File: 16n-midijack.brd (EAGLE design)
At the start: 248.9 x 120.7 mm, 108 parts, among them J1 PJ302M, J10 PJ302M, J11 PJ302M, J12 PJ302M, J13 PJ302M, J14 PJ302M, J15 PJ302M, J16 PJ302M, J2 PJ302M, J3 PJ302M, J4 PJ302M, J5 PJ302M, J6 PJ302M, J7 PJ302M, J8 PJ302M, J9 PJ302M, U1 MCP6004_SMD, U2 MCP6004_SMD, U3 MCP6004_SMD, U4 MCP6004_SMD, U5 MCP6004_SMD, U6 MCP6004_SMD, U7 MCP6004_SMD, U8 MCP6004_SMD

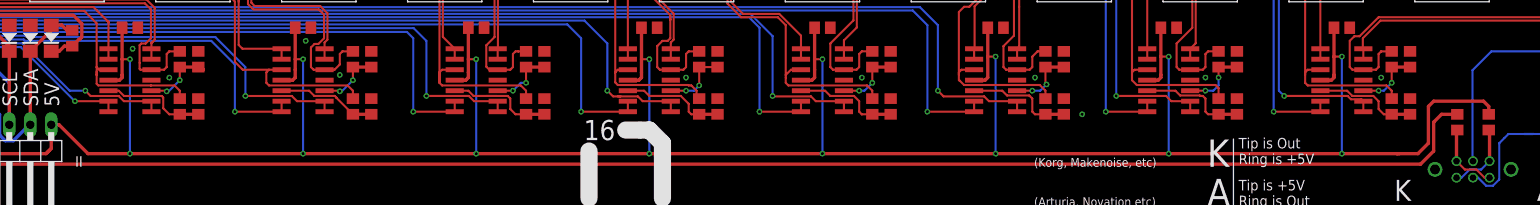
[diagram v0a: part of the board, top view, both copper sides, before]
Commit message: MIDI positive voltage should be 3V3 for Teensy 3.x. Fixed that.
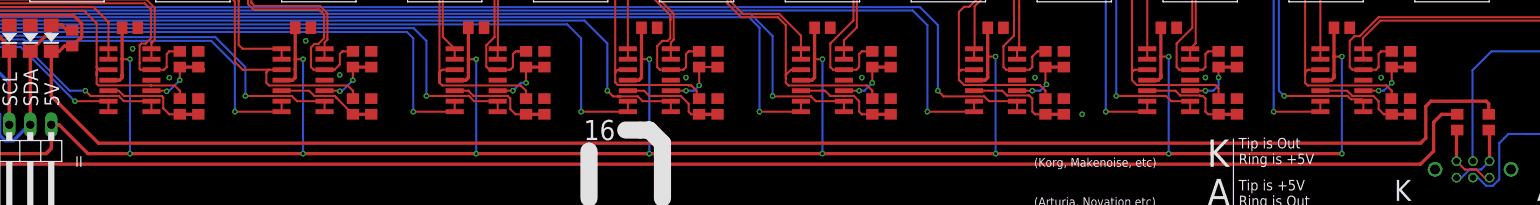
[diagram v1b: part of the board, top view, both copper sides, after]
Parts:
- R1, R2: value 220 -> 47
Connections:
- net +3V3: now also R1.2
- net +5V: no longer R1.2
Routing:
- net +3V3: track 80.7 -> 268.2 mm
- net +5V: track 761.3 -> 736.8 mm
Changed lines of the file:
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@@
 <?xml version="1.0" encoding="utf-8"?>
 <!DOCTYPE eagle SYSTEM "eagle.dtd">
-<eagle version="8.4.1">
+<eagle version="8.4.3">
 <drawing>
 <settings>
@@
 <setting verticaltext="up"/>
 </settings>
-<grid distance="12.5" unitdist="mil" unit="mil" style="dots" multiple="4" display="yes" altdistance="25" altunitdist="mil" altunit="mil"/>
+<grid distance="12.5" unitdist="mil" unit="mil" style="lines" multiple="4" display="yes" altdistance="25" altunitdist="mil" altunit="mil"/>
 <layers>
 <layer number="1" name="Top" color="4" fill="1" visible="yes" active="yes"/>
@@
 <element name="U$16" library="monome" package="RS6011SP600" value="SLIDEPOT-ALPS-60MM" x="25.4" y="63.5" rot="R270"/>
 <element name="U$17" library="monome" package="RS6011SP600" value="SLIDEPOT-ALPS-60MM" x="10.16" y="63.5" rot="R270"/>
-<element name="R1" library="rcl" library_urn="urn:adsk.eagle:library:334" package="R0805" package3d_urn="urn:adsk.eagle:package:23553/2" value="220" x="227.965" y="11.43" smashed="yes" rot="R90">
-<attribute name="VALUE" x="226.3775" y="13.6525" size="1.27" layer="27"/>
-</element>
-<element name="R2" library="rcl" library_urn="urn:adsk.eagle:library:334" package="R0805" package3d_urn="urn:adsk.eagle:package:23553/2" value="220" x="224.155" y="11.43" smashed="yes" rot="R90">
-<attribute name="VALUE" x="222.5675" y="13.6525" size="1.27" layer="27"/>
+<element name="R1" library="rcl" library_urn="urn:adsk.eagle:library:334" package="R0805" package3d_urn="urn:adsk.eagle:package:23553/2" value="47" x="227.965" y="11.43" smashed="yes" rot="R90">
+<attribute name="VALUE" x="227.0125" y="13.6525" size="1.27" layer="27"/>
+</element>
+<element name="R2" library="rcl" library_urn="urn:adsk.eagle:library:334" package="R0805" package3d_urn="urn:adsk.eagle:package:23553/2" value="47" x="224.155" y="11.43" smashed="yes" rot="R90">
+<attribute name="VALUE" x="223.2025" y="13.6525" size="1.27" layer="27"/>
 </element>
 <element name="JP1" library="SparkFun-Connectors" package="AUDIO-JACK" value="" x="245" y="15" rot="R180"/>
@@
 <contactref element="D2" pad="C"/>
 <contactref element="D4" pad="C"/>
-<wire x1="53.975" y1="20.015" x2="54.94" y2="20.015" width="0.4064" layer="1"/>
+<wire x1="54.94" y1="20.015" x2="53.975" y2="20.015" width="0.4064" layer="1"/>
 <wire x1="54.94" y1="20.015" x2="55.5625" y2="20.6375" width="0.4064" layer="1"/>
 <wire x1="55.5625" y1="20.6375" x2="56.5125" y2="20.6375" width="0.4064" layer="1"/>
@@
 <wire x1="46.0375" y1="20.0025" x2="46.0375" y2="20.015" width="0.8128" layer="1"/>
 <wire x1="37.465" y1="11.43" x2="46.0375" y2="20.0025" width="0.8128" layer="1"/>
+<contactref element="R1" pad="2"/>
+<wire x1="53.975" y1="20.015" x2="53.975" y2="14.605" width="0.4064" layer="1"/>
+<wire x1="53.975" y1="14.605" x2="59.69" y2="8.89" width="0.4064" layer="1"/>
+<wire x1="59.69" y1="8.89" x2="219.71" y2="8.89" width="0.4064" layer="1"/>
+<wire x1="219.71" y1="8.89" x2="220.345" y2="9.525" width="0.4064" layer="1"/>
+<wire x1="220.345" y1="13.335" x2="220.98" y2="13.97" width="0.4064" layer="1"/>
+<wire x1="220.98" y1="13.97" x2="227.6475" y2="13.97" width="0.4064" layer="1"/>
+<wire x1="227.6475" y1="13.97" x2="227.965" y2="13.6525" width="0.4064" layer="1"/>
+<wire x1="227.965" y1="13.6525" x2="227.965" y2="12.38" width="0.4064" layer="1"/>
+<wire x1="220.345" y1="9.525" x2="220.345" y2="13.335" width="0.4064" layer="1"/>
 </signal>
 <signal name="A0">
@@
 <signal name="+5V">
 <contactref element="U$1" pad="VUSB"/>
-<contactref element="R1" pad="2"/>
 <contactref element="II" pad="1"/>
 <wire x1="15.24" y1="8.89" x2="5.08" y2="19.05" width="0.4064" layer="1"/>
@@
 <wire x1="11.41" y1="98.5" x2="9.43" y2="96.52" width="0.6096" layer="16"/>
 <wire x1="9.43" y1="96.52" x2="9.2075" y2="96.52" width="0.6096" layer="16"/>
-<wire x1="227.33" y1="13.97" x2="227.965" y2="13.335" width="0.4064" layer="1"/>
-<wire x1="227.965" y1="13.335" x2="227.965" y2="12.38" width="0.4064" layer="1"/>
-<wire x1="221.2975" y1="13.97" x2="227.33" y2="13.97" width="0.4064" layer="1"/>
 <wire x1="62.55" y1="19.05" x2="62.55" y2="17.145" width="0.4064" layer="1"/>
 <wire x1="62.55" y1="19.05" x2="62.55" y2="22.86" width="0.4064" layer="1"/>
@@
 <wire x1="168.275" y1="7.62" x2="189.23" y2="7.62" width="0.4064" layer="1"/>
 <wire x1="189.23" y1="7.62" x2="210.185" y2="7.62" width="0.4064" layer="1"/>
-<wire x1="210.185" y1="7.62" x2="216.8525" y2="7.62" width="0.4064" layer="1"/>
-<wire x1="216.8525" y1="7.62" x2="217.17" y2="7.62" width="0.4064" layer="1"/>
-<wire x1="216.8525" y1="7.62" x2="219.3925" y2="7.62" width="0.4064" layer="1"/>
-<wire x1="219.3925" y1="7.62" x2="220.6625" y2="8.89" width="0.4064" layer="1"/>
-<wire x1="220.6625" y1="13.335" x2="221.2975" y2="13.97" width="0.4064" layer="1"/>
-<wire x1="220.6625" y1="8.89" x2="220.6625" y2="13.335" width="0.4064" layer="1"/>
 <wire x1="57.13" y1="98.5" x2="57.13" y2="98.405" width="0.4064" layer="16"/>
 <wire x1="57.13" y1="98.405" x2="55.245" y2="96.52" width="0.4064" layer="16"/>

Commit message: Make impedence jacks 1K.
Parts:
- R12, R17, R22, R27, R32, R37, R42, R45, R46, R47, R48, R49, R50, R51, R52, R7: value 100 -> 1K

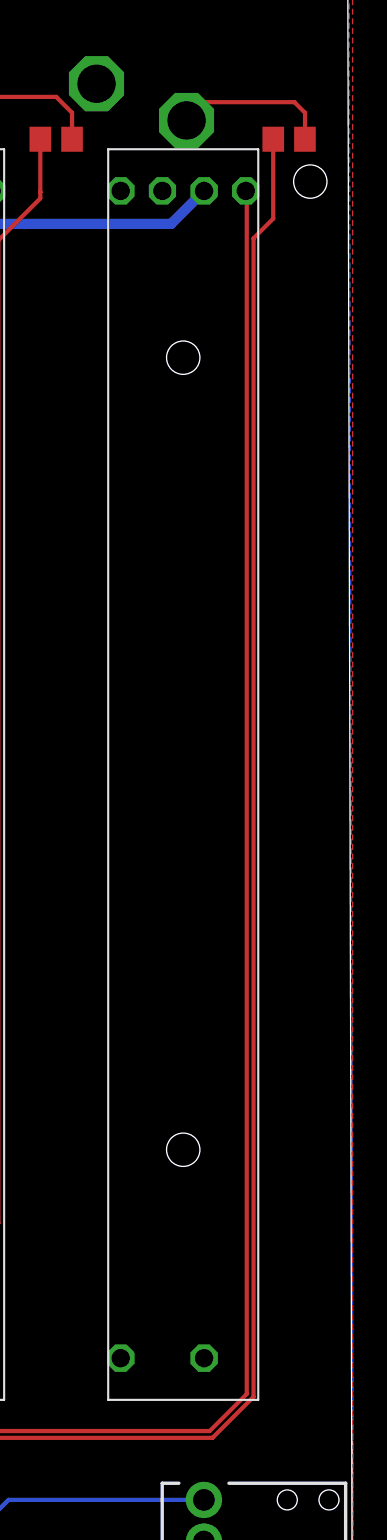
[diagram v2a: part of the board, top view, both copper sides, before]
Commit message: Move resistor so it won't interefere with standoff.
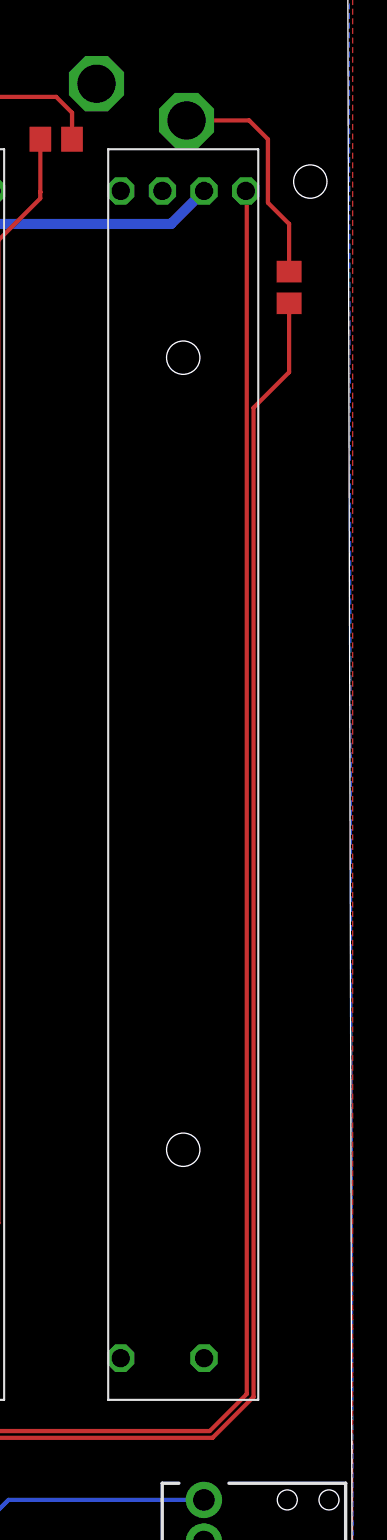
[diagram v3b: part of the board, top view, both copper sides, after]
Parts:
- moved R51 8.89 mm to (245.1, 92.7), turned to 90 degrees
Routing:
- net N$315: track 110.6 -> 101.2 mm
- net CV16: track 9.41 -> 13.8 mm
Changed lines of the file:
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@@
 <attribute name="VALUE" x="214.9475" y="99.06" size="1.27" layer="27"/>
 </element>
-<element name="R51" library="rcl" library_urn="urn:adsk.eagle:library:334" package="R0805" package3d_urn="urn:adsk.eagle:package:23553/2" value="1K" x="245.11" y="101.6" smashed="yes">
-<attribute name="VALUE" x="244.475" y="103.1875" size="1.27" layer="27"/>
+<element name="R51" library="rcl" library_urn="urn:adsk.eagle:library:334" package="R0805" package3d_urn="urn:adsk.eagle:package:23553/2" value="1K" x="245.11" y="92.71" smashed="yes" rot="R90">
+<attribute name="VALUE" x="244.1575" y="88.9" size="1.27" layer="27"/>
 </element>
 <element name="R52" library="rcl" library_urn="urn:adsk.eagle:library:334" package="R0805" package3d_urn="urn:adsk.eagle:package:23553/2" value="1K" x="48.26" y="101.6" smashed="yes">
@@
 <contactref element="J16" pad="TIP"/>
 <contactref element="R51" pad="2"/>
-<wire x1="238.96" y1="102.7275" x2="240.055" y2="103.8225" width="0.254" layer="1"/>
-<wire x1="245.4275" y1="103.8225" x2="246.0625" y2="103.1875" width="0.254" layer="1"/>
-<wire x1="246.0625" y1="103.1875" x2="246.0625" y2="101.6025" width="0.254" layer="1"/>
-<wire x1="246.0625" y1="101.6025" x2="246.06" y2="101.6" width="0.254" layer="1"/>
-<wire x1="240.055" y1="103.8225" x2="245.4275" y2="103.8225" width="0.254" layer="1"/>
+<wire x1="238.96" y1="102.7275" x2="242.7125" y2="102.7275" width="0.254" layer="1"/>
+<wire x1="242.7125" y1="102.7275" x2="243.84" y2="101.6" width="0.254" layer="1"/>
+<wire x1="243.84" y1="101.6" x2="243.84" y2="97.79" width="0.254" layer="1"/>
+<wire x1="243.84" y1="97.79" x2="245.11" y2="96.52" width="0.254" layer="1"/>
+<wire x1="245.11" y1="96.52" x2="245.11" y2="93.66" width="0.254" layer="1"/>
 </signal>
 <signal name="CV15">
@@
 <contactref element="R51" pad="1"/>
 <wire x1="212.785" y1="20.32" x2="212.785" y2="19.05" width="0.254" layer="1"/>
-<wire x1="244.16" y1="101.6" x2="244.16" y2="96.84" width="0.254" layer="1"/>
-<wire x1="244.16" y1="96.84" x2="242.9764" y2="95.6564" width="0.254" layer="1"/>
-<wire x1="242.9764" y1="95.6564" x2="242.9764" y2="26.1841625" width="0.254" layer="1"/>
-<wire x1="242.9764" y1="26.1841625" x2="240.5158375" y2="23.7236" width="0.254" layer="1"/>
+<wire x1="240.5158375" y1="23.7236" x2="242.9764" y2="26.1841625" width="0.254" layer="1"/>
 <wire x1="214.8586" y1="23.7236" x2="212.725" y2="21.59" width="0.254" layer="1"/>
 <wire x1="212.725" y1="21.59" x2="212.725" y2="20.38" width="0.254" layer="1"/>
 <wire x1="212.725" y1="20.38" x2="212.785" y2="20.32" width="0.254" layer="1"/>
 <wire x1="240.5158375" y1="23.7236" x2="214.8586" y2="23.7236" width="0.254" layer="1"/>
+<wire x1="242.9764" y1="85.4964" x2="245.11" y2="87.63" width="0.254" layer="1"/>
+<wire x1="245.11" y1="87.63" x2="245.11" y2="91.76" width="0.254" layer="1"/>
+<wire x1="242.9764" y1="26.1841625" x2="242.9764" y2="85.4964" width="0.254" layer="1"/>
 </signal>
 <signal name="N$314">

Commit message: Add 2x8 header for I2C; add fiducials.
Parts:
- added FID1, FID2: FIDUCIAL, adafruit:FIDUCIAL_1MM
- II: device pinhead:1X04/90 -> pinhead:2X04/90
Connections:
- net +5V: now also II.2
- net GND: now also II.7, II.8; no longer II.4
- net SCL: now also II.5, II.6; no longer II.3
- net SDA: now also II.3, II.4; no longer II.2
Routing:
- net SCL: track 38.1 -> 35.5 mm
- net +5V: track 736.8 -> 739.3 mm
- net SDA: track 42.2 -> 43.8 mm
- net +3V3: track 268.2 -> 269.1 mm
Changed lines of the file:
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@@
 <text x="235.585" y="1.905" size="2.54" layer="26" ratio="12" rot="MR0">A</text>
 <text x="218.1225" y="1.905" size="2.54" layer="26" ratio="12" rot="MR0">K</text>
-<text x="49.8475" y="13.335" size="1.778" layer="25" rot="R90">SCL</text>
-<text x="52.3875" y="13.335" size="1.778" layer="25" rot="R90">SDA</text>
-<text x="54.9275" y="13.335" size="1.778" layer="25" rot="R90">5V</text>
-<text x="47.3075" y="13.335" size="1.778" layer="25" rot="R90">GND</text>
+<text x="48.895" y="14.9225" size="1.524" layer="25" rot="R90" align="center-left">SCL</text>
+<text x="51.435" y="14.9225" size="1.524" layer="25" rot="R90" align="center-left">SDA</text>
+<text x="53.975" y="14.9225" size="1.524" layer="25" rot="R90" align="center-left">5V</text>
+<text x="46.355" y="14.9225" size="1.524" layer="25" rot="R90" align="center-left">GND</text>
 <polygon width="0.4064" layer="25">
 <vertex x="43.18" y="9.2075"/>
@@
 <element name="JP1" library="SparkFun-Connectors" package="AUDIO-JACK" value="" x="245" y="15" rot="R180"/>
 <element name="S1" library="SparkFun-Electromechanical" package="EG2211" value="" x="226.06" y="5.715" rot="R90"/>
-<element name="II" library="pinhead" library_urn="urn:adsk.eagle:library:325" package="1X04/90" package3d_urn="urn:adsk.eagle:package:22404/1" value="" x="50.165" y="7.3025" smashed="yes" rot="R180">
-<attribute name="NAME" x="57.785" y="7.3025" size="1.27" layer="25" ratio="10" rot="R180"/>
-<attribute name="VALUE" x="43.015" y="10.445" size="1.27" layer="27" rot="R270"/>
-</element>
 <element name="R3" library="rcl" library_urn="urn:adsk.eagle:library:334" package="R0805" package3d_urn="urn:adsk.eagle:package:23553/2" value="4K7" x="56.515" y="21.59" smashed="yes" rot="R270">
 <attribute name="VALUE" x="54.9275" y="24.13" size="1.27" layer="27"/>
@@
 <attribute name="VALUE" x="47.3075" y="99.06" size="1.27" layer="27"/>
 </element>
+<element name="II" library="pinhead" library_urn="urn:adsk.eagle:library:325" package="2X04/90" package3d_urn="urn:adsk.eagle:package:22465/2" value="" x="50.165" y="7.3025" rot="R180"/>
+<element name="FID1" library="adafruit" library_urn="urn:adsk.eagle:library:420" package="FIDUCIAL_1MM" value="FIDUCIAL" x="2.54" y="115.57"/>
+<element name="FID2" library="adafruit" library_urn="urn:adsk.eagle:library:420" package="FIDUCIAL_1MM" value="FIDUCIAL" x="246.38" y="6.35"/>
 </elements>
 <signals>
@@
 <contactref element="U$17" pad="3"/>
 <contactref element="JP1" pad="SLEEVE"/>
-<contactref element="II" pad="4"/>
 <contactref element="D1" pad="A"/>
 <contactref element="D3" pad="A"/>
@@
 <via x="68.2625" y="16.8275" extent="1-16" drill="0.35"/>
 <via x="63.8175" y="20.32" extent="1-16" drill="0.35"/>
+<contactref element="II" pad="7"/>
+<contactref element="II" pad="8"/>
 </signal>
 <signal name="VIN">
@@
 <wire x1="37.465" y1="11.43" x2="46.0375" y2="20.0025" width="0.8128" layer="1"/>
 <contactref element="R1" pad="2"/>
-<wire x1="53.975" y1="20.015" x2="53.975" y2="14.605" width="0.4064" layer="1"/>
-<wire x1="53.975" y1="14.605" x2="59.69" y2="8.89" width="0.4064" layer="1"/>
-<wire x1="59.69" y1="8.89" x2="219.71" y2="8.89" width="0.4064" layer="1"/>
-<wire x1="219.71" y1="8.89" x2="220.345" y2="9.525" width="0.4064" layer="1"/>
+<wire x1="53.975" y1="16.8275" x2="53.975" y2="20.015" width="0.4064" layer="1"/>
+<wire x1="220.345" y1="9.525" x2="219.71" y2="8.89" width="0.4064" layer="1"/>
 <wire x1="220.345" y1="13.335" x2="220.98" y2="13.97" width="0.4064" layer="1"/>
 <wire x1="220.98" y1="13.97" x2="227.6475" y2="13.97" width="0.4064" layer="1"/>
@@
 <wire x1="227.965" y1="13.6525" x2="227.965" y2="12.38" width="0.4064" layer="1"/>
 <wire x1="220.345" y1="9.525" x2="220.345" y2="13.335" width="0.4064" layer="1"/>
+<wire x1="58.1025" y1="8.89" x2="55.5625" y2="11.43" width="0.4064" layer="1"/>
+<wire x1="219.71" y1="8.89" x2="58.1025" y2="8.89" width="0.4064" layer="1"/>
+<wire x1="55.5625" y1="11.43" x2="55.5625" y2="15.24" width="0.4064" layer="1"/>
+<wire x1="55.5625" y1="15.24" x2="53.975" y2="16.8275" width="0.4064" layer="1"/>
 </signal>
 <signal name="A0">
@@
 <signal name="+5V">
 <contactref element="U$1" pad="VUSB"/>
-<contactref element="II" pad="1"/>
 <wire x1="15.24" y1="8.89" x2="5.08" y2="19.05" width="0.4064" layer="1"/>
 <wire x1="33.02" y1="8.89" x2="34.29" y2="7.62" width="0.4064" layer="1"/>
@@
 <wire x1="15.24" y1="8.89" x2="33.02" y2="8.89" width="0.4064" layer="1"/>
 <wire x1="34.29" y1="7.62" x2="53.34" y2="7.62" width="0.4064" layer="1"/>
-<wire x1="53.975" y1="8.255" x2="53.975" y2="11.1125" width="0.4064" layer="1"/>
-<wire x1="53.975" y1="8.255" x2="53.49875" y2="7.77875" width="0.4064" layer="1"/>
+<wire x1="53.49875" y1="7.77875" x2="53.975" y2="8.255" width="0.4064" layer="1"/>
 <contactref element="U$2" pad="1"/>
 <contactref element="U$3" pad="1"/>
@@
 <wire x1="209.235" y1="16.83" x2="208.915" y2="16.51" width="0.4064" layer="1"/>
 <wire x1="208.915" y1="16.51" x2="207.585" y2="16.51" width="0.4064" layer="1"/>
-<wire x1="53.975" y1="11.1125" x2="54.9275" y2="11.1125" width="0.4064" layer="1"/>
-<wire x1="54.9275" y1="11.1125" x2="58.42" y2="7.62" width="0.4064" layer="1"/>
-<wire x1="58.42" y1="7.62" x2="63.5" y2="7.62" width="0.4064" layer="1"/>
-<wire x1="63.5" y1="7.62" x2="84.455" y2="7.62" width="0.4064" layer="1"/>
+<wire x1="84.455" y1="7.62" x2="63.5" y2="7.62" width="0.4064" layer="1"/>
 <wire x1="84.455" y1="7.62" x2="105.41" y2="7.62" width="0.4064" layer="1"/>
 <wire x1="105.41" y1="7.62" x2="126.365" y2="7.62" width="0.4064" layer="1"/>
@@
 <via x="210.185" y="19.3675" extent="1-16" drill="0.35"/>
 <wire x1="210.185" y1="19.3675" x2="209.235" y2="19.3675" width="0.254" layer="1"/>
+<contactref element="II" pad="1"/>
+<contactref element="II" pad="2"/>
+<wire x1="53.975" y1="8.255" x2="53.975" y2="11.1125" width="0.4064" layer="1"/>
+<wire x1="57.4675" y1="7.62" x2="53.975" y2="11.1125" width="0.4064" layer="1"/>
+<wire x1="63.5" y1="7.62" x2="57.4675" y2="7.62" width="0.4064" layer="1"/>
+<wire x1="53.975" y1="11.1125" x2="53.975" y2="13.6525" width="0.4064" layer="1"/>
 </signal>
 <signal name="N$3">
@@
 </signal>
 <signal name="SDA">
-<contactref element="II" pad="2"/>
 <contactref element="R3" pad="1"/>
 <contactref element="D1" pad="C"/>
 <contactref element="D2" pad="A"/>
-<wire x1="53.975" y1="22.555" x2="51.435" y2="20.015" width="0.4064" layer="1"/>
+<wire x1="51.435" y1="20.015" x2="53.975" y2="22.555" width="0.4064" layer="1"/>
 <wire x1="53.975" y1="23.165" x2="53.975" y2="22.555" width="0.4064" layer="1"/>
-<wire x1="51.435" y1="20.015" x2="51.435" y2="11.1125" width="0.4064" layer="1"/>
 <wire x1="56.515" y1="22.54" x2="55.8825" y2="22.54" width="0.4064" layer="1"/>
 <wire x1="55.8825" y1="22.54" x2="55.245" y2="23.1775" width="0.4064" layer="1"/>
@@
 <wire x1="53.9875" y1="23.1775" x2="53.975" y2="23.165" width="0.4064" layer="1"/>
 <contactref element="U$1" pad="30"/>
-<wire x1="47.7266" y1="12.35846875" x2="47.7266" y2="9.86653125" width="0.4064" layer="16"/>
-<wire x1="47.7266" y1="9.86653125" x2="48.41103125" y2="9.1821" width="0.4064" layer="16"/>
-<wire x1="48.41103125" y1="9.1821" x2="49.37896875" y2="9.1821" width="0.4064" layer="16"/>
+<wire x1="48.41103125" y1="9.1821" x2="47.7266" y2="9.86653125" width="0.4064" layer="16"/>
 <wire x1="30.48" y1="16.51" x2="31.40355" y2="16.51" width="0.4064" layer="16"/>
 <wire x1="31.40355" y1="16.51" x2="32.54655" y2="15.367" width="0.4064" layer="16"/>
-<wire x1="44.71806875" y1="15.367" x2="47.7266" y2="12.35846875" width="0.4064" layer="16"/>
-<wire x1="51.30936875" y1="11.1125" x2="51.435" y2="11.1125" width="0.4064" layer="16"/>
-<wire x1="32.54655" y1="15.367" x2="44.71806875" y2="15.367" width="0.4064" layer="16"/>
-<wire x1="49.37896875" y1="9.1821" x2="51.30936875" y2="11.1125" width="0.4064" layer="16"/>
+<contactref element="II" pad="3"/>
+<contactref element="II" pad="4"/>
+<wire x1="32.54655" y1="15.367" x2="47.498" y2="15.367" width="0.4064" layer="16"/>
+<wire x1="47.498" y1="15.367" x2="47.7266" y2="15.1384" width="0.4064" layer="16"/>
+<wire x1="47.7266" y1="15.1384" x2="47.7266" y2="9.86653125" width="0.4064" layer="16"/>
+<wire x1="51.435" y1="13.6525" x2="51.435" y2="20.015" width="0.4064" layer="1"/>
+<wire x1="51.435" y1="13.6525" x2="51.435" y2="11.1125" width="0.4064" layer="16"/>
+<wire x1="51.435" y1="11.1125" x2="49.5046" y2="9.1821" width="0.4064" layer="16"/>
+<wire x1="49.5046" y1="9.1821" x2="48.41103125" y2="9.1821" width="0.4064" layer="16"/>
 </signal>
 <signal name="SCL">
-<contactref element="II" pad="3"/>
 <contactref element="R4" pad="1"/>
 <wire x1="34.29" y1="17.78" x2="47.3075" y2="17.78" width="0.4064" layer="16"/>
 <contactref element="D3" pad="C"/>
 <contactref element="D4" pad="A"/>
-<wire x1="48.895" y1="16.1925" x2="48.895" y2="11.1125" width="0.4064" layer="16"/>
 <wire x1="47.3075" y1="17.78" x2="48.895" y2="16.1925" width="0.4064" layer="16"/>
 <wire x1="46.355" y1="23.165" x2="48.895" y2="20.625" width="0.4064" layer="1"/>
-<wire x1="48.895" y1="20.625" x2="48.895" y2="20.015" width="0.4064" layer="1"/>
-<wire x1="48.895" y1="20.015" x2="48.895" y2="11.1125" width="0.4064" layer="1"/>
+<wire x1="48.895" y1="20.015" x2="48.895" y2="20.625" width="0.4064" layer="1"/>
 <wire x1="43.815" y1="22.54" x2="44.4475" y2="22.54" width="0.4064" layer="1"/>
 <wire x1="44.4475" y1="22.54" x2="45.085" y2="23.1775" width="0.4064" layer="1"/>
@@
 <contactref element="U$1" pad="29"/>
 <wire x1="33.02" y1="16.51" x2="34.29" y2="17.78" width="0.4064" layer="16"/>
+<contactref element="II" pad="5"/>
+<contactref element="II" pad="6"/>
+<wire x1="48.895" y1="16.1925" x2="48.895" y2="13.6525" width="0.4064" layer="16"/>
+<wire x1="48.895" y1="13.6525" x2="48.895" y2="11.1125" width="0.4064" layer="16"/>
+<wire x1="48.895" y1="13.6525" x2="48.895" y2="20.015" width="0.4064" layer="1"/>
 </signal>
 <signal name="W0">
